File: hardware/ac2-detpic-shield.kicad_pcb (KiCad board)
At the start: 2 copper layers, 99.1 x 99.1 mm, 43 parts, among them Q1 VN2222, Q2 VN2222, SW1 SW_DIP_x04, U1 25LC040A, U2 LTD-4708JR, U3 TC74

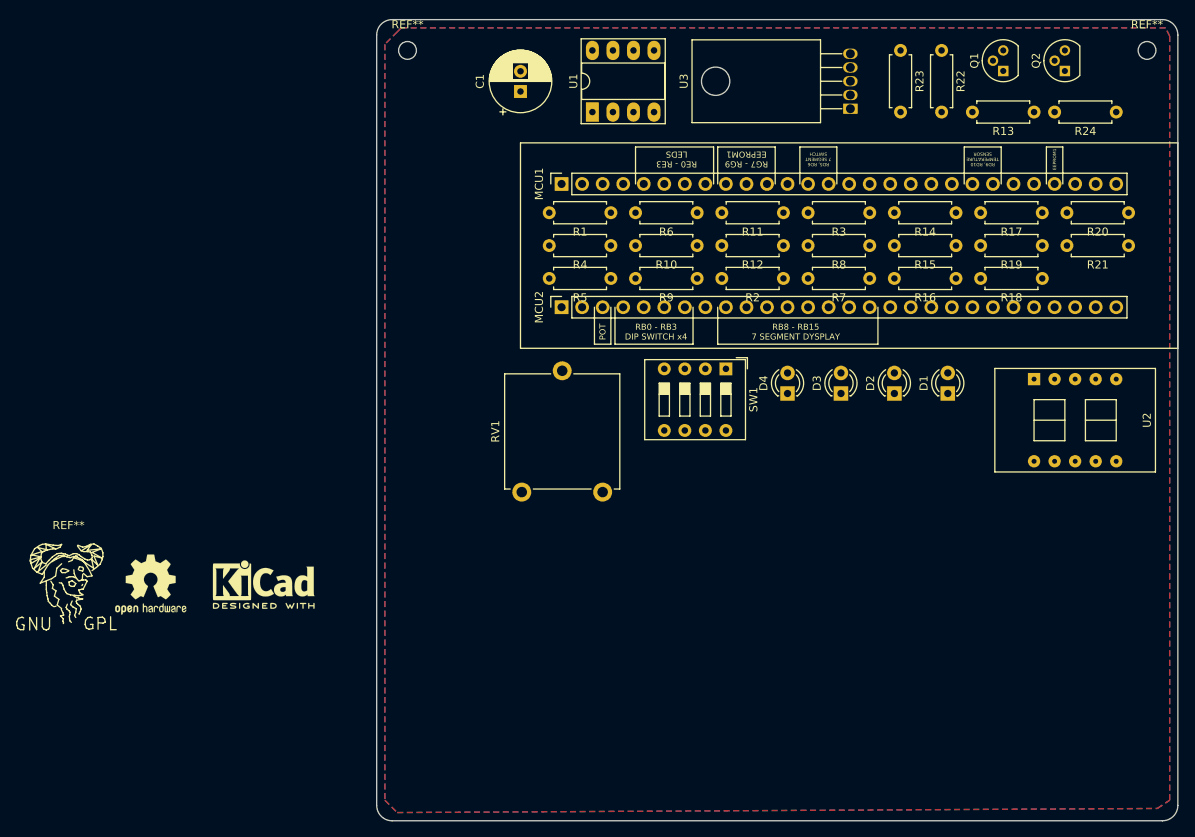
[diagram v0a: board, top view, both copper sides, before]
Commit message: pcb completed + gerbers exported
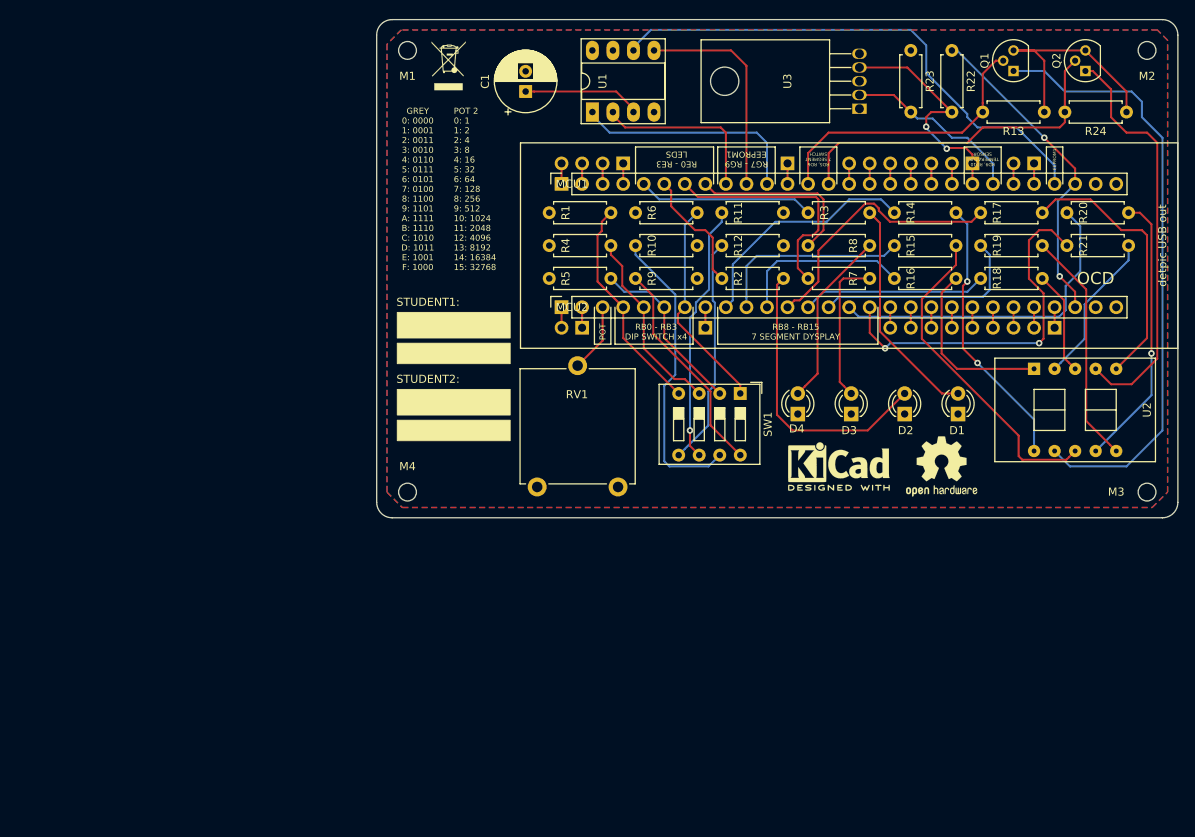
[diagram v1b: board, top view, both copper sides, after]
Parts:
- removed the REF** at (88.9, 94.0)
- removed the REF** at (130.8, 29.2)
- added J1: HEADER, Connector_PinHeader_2.54mm:PinHeader_1x04_P2.54mm_Vertical, B.Cu at (157.5, 43.2)
- added J2: HEADER, Connector_PinHeader_2.54mm:PinHeader_1x01_P2.54mm_Vertical, B.Cu at (177.8, 43.2)
- added J3: HEADER, Connector_PinHeader_2.54mm:PinHeader_1x07_P2.54mm_Vertical, B.Cu at (200.7, 43.2)
- added J4: HEADER, Connector_PinHeader_2.54mm:PinHeader_1x02_P2.54mm_Vertical, B.Cu at (208.3, 43.2)
- added J5: HEADER, Connector_PinHeader_2.54mm:PinHeader_1x02_P2.54mm_Vertical, B.Cu at (152.4, 63.5)
- added J6: HEADER, Connector_PinHeader_2.54mm:PinHeader_1x01_P2.54mm_Vertical, B.Cu at (167.6, 63.5)
- added J7: HEADER, Connector_PinHeader_2.54mm:PinHeader_1x09_P2.54mm_Vertical, B.Cu at (210.8, 63.5)
- added M1: M1, MountingHole:MountingHole_2.2mm_M2, F.Cu at (130.8, 29.2)
- added M3: MountingHole_2.2mm_M2, MountingHole:MountingHole_2.2mm_M2, F.Cu at (222.2, 83.8)
- added M4: MountingHole_2.2mm_M2, MountingHole:MountingHole_2.2mm_M2, F.Cu at (130.8, 83.8)
- added REF**: WEEE-Logo_4.2x6mm_SilkScreen, Symbol:WEEE-Logo_4.2x6mm_SilkScreen, F.Cu at (135.9, 31.1)
- M2: renamed from REF**; value MountingHole_2.2mm_M2 -> M2
- SW1: value SW_DIP_x04 -> DIP SWITCH x4
- moved REF** 98.9 mm to (196.8, 80.6)
- moved REF** 72.6 mm to (184.2, 80.6)
- moved R7 7.62 mm to (180.3, 57.4), turned to 0 degrees
- moved R8 7.62 mm to (180.3, 53.3), turned to 0 degrees
- moved SW1 3.53 mm to (172.0, 71.6)
- moved D1 2.84 mm to (198.9, 74.2)
- moved D3 2.84 mm to (185.7, 74.2)
- moved D2 2.84 mm to (192.3, 74.2)
- moved D4 2.84 mm to (179.1, 74.2)
- moved Q2 2.54 mm to (214.6, 31.8)
- moved RV1 2.01 mm to (156.8, 83.2)
- moved Q1 1.27 mm to (205.7, 31.8)
- moved R13 1.27 mm to (209.6, 36.8)
- moved R22 1.27 mm to (198.1, 29.2)
- moved R24 1.27 mm to (219.7, 36.8)
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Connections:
- MCU1 pad 27: /+5V_EXT -> /+5V_EXT1
- MCU2 pad 27: /+5V_EXT -> /+5V_EXT2
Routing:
- net Net-(Q1-Pad1): track 0.00 -> 75.1 mm
- net /RG6: track 0.00 -> 64.8 mm
- net Net-(Q2-Pad1): track 0.00 -> 51.0 mm
- net /RB15: track 0.00 -> 44.9 mm, vias 0 -> 2
- net /RD5: track 0.00 -> 42.7 mm
- net /RB14: track 0.00 -> 41.1 mm
- net Net-(R15-Pad1): track 0.00 -> 40.4 mm
- net /+3.3V: track 0.00 -> 40.2 mm, vias 0 -> 2
- net Net-(R10-Pad2): track 0.00 -> 37.0 mm
- net Net-(D2-Pad2): track 0.00 -> 35.7 mm
- net /RD6: track 0.00 -> 35.4 mm
- net Net-(R20-Pad1): track 0.00 -> 34.3 mm, vias 0 -> 1
- net Net-(R14-Pad1): track 0.00 -> 33.9 mm, vias 0 -> 2
- net Net-(R17-Pad1): track 0.00 -> 33.6 mm
- net /RB11: track 0.00 -> 33.0 mm
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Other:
- board size 99.1 x 99.1 mm -> 99.1 x 61.6 mm
- board text added: "GREY 0: 0000 1: 0001 2: 0011 3: 0010 4: 0110 5: 0111 6: 0101 7: 0100 8: 1100 9: 1101 A: 1111 B: 1110 C: 1010 D: 1011 E: 1001 F: 1000"
- board text added: "In case this board is lost, deliver it to someone at the Electronics, Telecomunications and Informatics department's secretary"
- board text added: "Licence: MIT Copyright 2019 Diogo Correia This shield extends the detpic32 development board created at DETI UA This PCB is intended to be updated has the subject evolves Feel free to request changes or make them yourself Consider contributing your changes to the repo"
- board text added: "OCD"
- board text added: "POT 2 0: 1 1: 2 2: 4 3: 8 4: 16 5: 32 6: 64 7: 128 8: 256 9: 512 10: 1024 11: 2048 12: 4096 13: 8192 14: 16384 15: 32768"
- board text added: "STUDENT1:"
- board text added: "STUDENT2:"
- board text added: "Your can find more information here https://github.com/dvcorreia/ac2-detpic-shield"
- board text added: "detpic USB out"
